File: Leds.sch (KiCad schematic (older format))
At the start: 1 part

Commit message: version preliminar de la etapa de alimentacion
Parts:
- gave numbers to parts that had none: 1
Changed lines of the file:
@@
 LIBS:Sensores
 LIBS:Reles
+LIBS:Reguladores
+LIBS:Transistores
 LIBS:Wifi_PB-cache
 EELAYER 26 0
@@
 $Descr A4 11693 8268
 encoding utf-8
-Sheet 9 11
+Sheet 9 15
 Title ""
 Date "2017-01-15"
@@
 $EndDescr
 $Comp
-L R R?
+L R R38
 U 1 1 587C019B
 P 5250 3800
-F 0 "R?" H 5320 3846 50  0000 L CNN
+F 0 "R38" H 5320 3846 50  0000 L CNN
 F 1 "R" H 5320 3755 50  0000 L CNN
-F 2 "" V 5180 3800 50  0000 C CNN
+F 2 "" V 5180 3800 50  0001 C CNN
 F 3 "" H 5250 3800 50  0000 C CNN
 	1    5250 3800

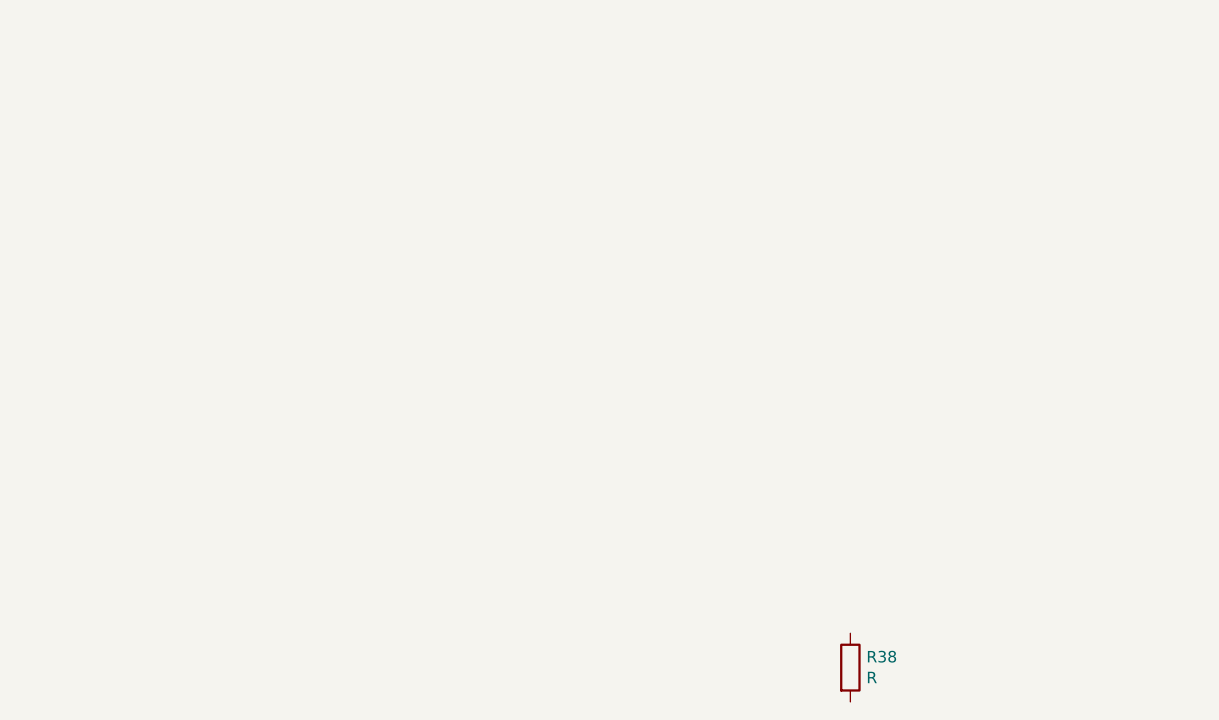
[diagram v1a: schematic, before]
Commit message: asignacion inicial de huellas
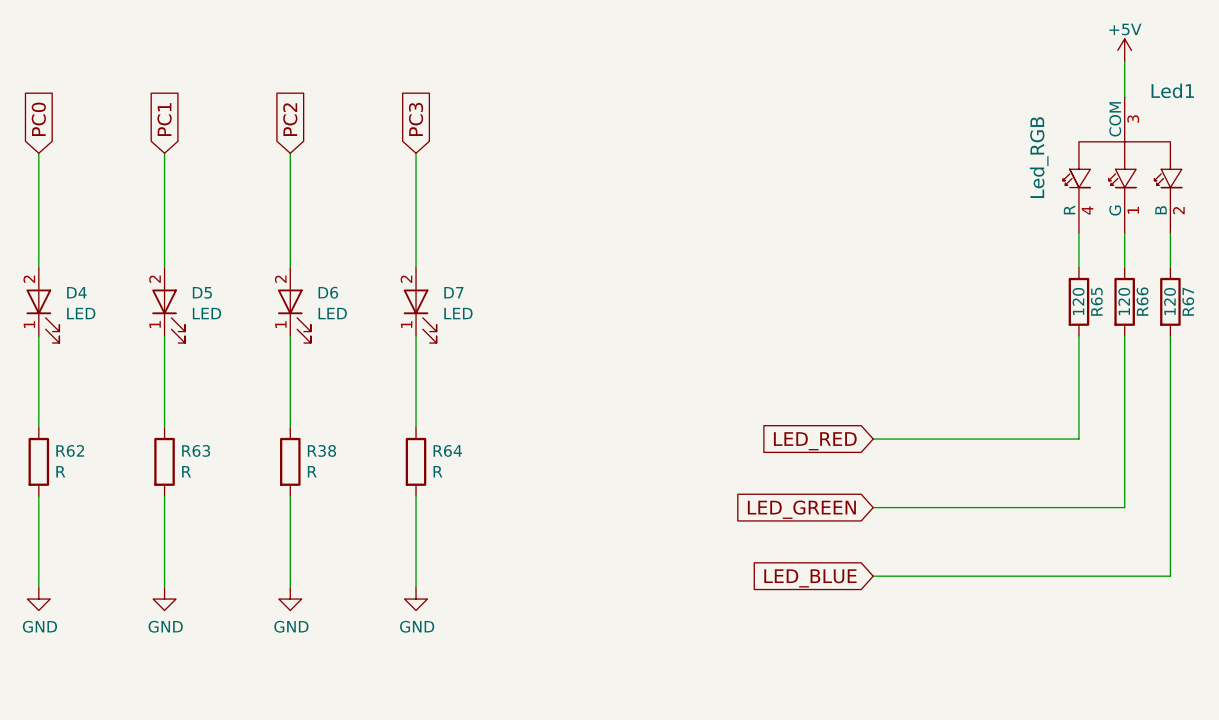
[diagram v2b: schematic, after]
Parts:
- added D4, D5, D6, D7: LED, LEDs:LED_0805, symbol LED
- added Led1: Led_RGB, Leds:LED_RGB_5mm_G_B_COM_R_Anodo_comun, symbol Led_RGB_Anodo_Comun
- added R62, R63, R64: R, Resistencias:R_0805, symbol R
- added R65, R66, R67: 120, Resistencias:R_0805, symbol R
- R38: footprint (none) -> Resistencias:R_0805
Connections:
- net at R38.1: now also D6.1 (K)
- net GND: now reaches R38.2
- net GND: now also R62.2, R63.2, R64.2
- new net: D7.1 (K), R64.1
- new net: D4.1 (K), R62.1
- new net: D5.1 (K), R63.1
- new net: Led1.1 (G), R66.1
- new net: Led1.2 (B), R67.1
- new net: Led1.4 (R), R65.1
- new net +5V: Led1.3 (COM)
- new net LED_BLUE: R67.2
- new net LED_GREEN: R66.2
- new net LED_RED: R65.2
- new net PC0: D4.2 (A)
- new net PC1: D5.2 (A)
- new net PC2: D6.2 (A)
- new net PC3: D7.2 (A)
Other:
- moved on the sheet: R38

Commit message: place inicial sobre la pcb
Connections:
- net GND: now also D4.1 (K), D5.1 (K), D6.1 (K), D7.1 (K); no longer R38.2, R62.2, R63.2, R64.2
- net PC0: now also R62.1; no longer D4.2 (A)
- net PC1: now also R63.1; no longer D5.2 (A)
- net PC2: now also R38.1; no longer D6.2 (A)
- net PC3: now also R64.1; no longer D7.2 (A)
- new net: D6.2 (A), R38.2
- new net: D7.2 (A), R64.2
- new net: D4.2 (A), R62.2
- new net: D5.2 (A), R63.2
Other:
- moved on the sheet: D4, D5, D6, D7, R38, R62, R63, R64
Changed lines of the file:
@@
 L R R38
 U 1 1 587C019B
-P 2800 2900
-F 0 "R38" H 2870 2946 50  0000 L CNN
-F 1 "R" H 2870 2855 50  0000 L CNN
-F 2 "Resistencias:R_0805" V 2730 2900 50  0001 C CNN
-F 3 "" H 2800 2900 50  0000 C CNN
-	1    2800 2900
+P 2800 2200
+F 0 "R38" H 2870 2246 50  0000 L CNN
+F 1 "R" H 2870 2155 50  0000 L CNN
+F 2 "Resistencias:R_0805" V 2730 2200 50  0001 C CNN
+F 3 "" H 2800 2200 50  0000 C CNN
+	1    2800 2200
 	1    0    0    -1
 $EndComp
@@
 L LED D6
 U 1 1 58911235
-P 2800 2200
-F 0 "D6" V 2838 2083 50  0000 R CNN
-F 1 "LED" V 2747 2083 50  0000 R CNN
-F 2 "LEDs:LED_0805" H 2800 2200 50  0001 C CNN
-F 3 "" H 2800 2200 50  0001 C CNN
-	1    2800 2200
+P 2800 2900
+F 0 "D6" V 2838 2783 50  0000 R CNN
+F 1 "LED" V 2747 2783 50  0000 R CNN
+F 2 "LEDs:LED_0805" H 2800 2900 50  0001 C CNN
+F 3 "" H 2800 2900 50  0001 C CNN
+	1    2800 2900
 	0    -1   -1   0
 $EndComp
@@
 L R R64
 U 1 1 5891178E
-P 3350 2900
-F 0 "R64" H 3420 2946 50  0000 L CNN
-F 1 "R" H 3420 2855 50  0000 L CNN
-F 2 "Resistencias:R_0805" V 3280 2900 50  0001 C CNN
-F 3 "" H 3350 2900 50  0000 C CNN
-	1    3350 2900
+P 3350 2200
+F 0 "R64" H 3420 2246 50  0000 L CNN
+F 1 "R" H 3420 2155 50  0000 L CNN
+F 2 "Resistencias:R_0805" V 3280 2200 50  0001 C CNN
+F 3 "" H 3350 2200 50  0000 C CNN
+	1    3350 2200
 	1    0    0    -1
 $EndComp
@@
 L LED D7
 U 1 1 58911795
-P 3350 2200
-F 0 "D7" V 3388 2083 50  0000 R CNN
-F 1 "LED" V 3297 2083 50  0000 R CNN
-F 2 "LEDs:LED_0805" H 3350 2200 50  0001 C CNN
-F 3 "" H 3350 2200 50  0001 C CNN
-	1    3350 2200
+P 3350 2900
+F 0 "D7" V 3388 2783 50  0000 R CNN
+F 1 "LED" V 3297 2783 50  0000 R CNN
+F 2 "LEDs:LED_0805" H 3350 2900 50  0001 C CNN
+F 3 "" H 3350 2900 50  0001 C CNN
+	1    3350 2900
 	0    -1   -1   0
 $EndComp
@@
 L R R62
 U 1 1 589119C4
-P 1700 2900
-F 0 "R62" H 1770 2946 50  0000 L CNN
-F 1 "R" H 1770 2855 50  0000 L CNN
-F 2 "Resistencias:R_0805" V 1630 2900 50  0001 C CNN
-F 3 "" H 1700 2900 50  0000 C CNN
-	1    1700 2900
+P 1700 2200
+F 0 "R62" H 1770 2246 50  0000 L CNN
+F 1 "R" H 1770 2155 50  0000 L CNN
+F 2 "Resistencias:R_0805" V 1630 2200 50  0001 C CNN
+F 3 "" H 1700 2200 50  0000 C CNN
+	1    1700 2200
 	1    0    0    -1
 $EndComp
@@
 L LED D4
 U 1 1 589119CB
-P 1700 2200
-F 0 "D4" V 1738 2083 50  0000 R CNN
-F 1 "LED" V 1647 2083 50  0000 R CNN
-F 2 "LEDs:LED_0805" H 1700 2200 50  0001 C CNN
-F 3 "" H 1700 2200 50  0001 C CNN
-	1    1700 2200
+P 1700 2900
+F 0 "D4" V 1738 2783 50  0000 R CNN
+F 1 "LED" V 1647 2783 50  0000 R CNN
+F 2 "LEDs:LED_0805" H 1700 2900 50  0001 C CNN
+F 3 "" H 1700 2900 50  0001 C CNN
+	1    1700 2900
 	0    -1   -1   0
 $EndComp
@@
 L R R63
 U 1 1 589119D2
-P 2250 2900
-F 0 "R63" H 2320 2946 50  0000 L CNN
-F 1 "R" H 2320 2855 50  0000 L CNN
-F 2 "Resistencias:R_0805" V 2180 2900 50  0001 C CNN
-F 3 "" H 2250 2900 50  0000 C CNN
-	1    2250 2900
+P 2250 2200
+F 0 "R63" H 2320 2246 50  0000 L CNN
+F 1 "R" H 2320 2155 50  0000 L CNN
+F 2 "Resistencias:R_0805" V 2180 2200 50  0001 C CNN
+F 3 "" H 2250 2200 50  0000 C CNN
+	1    2250 2200
 	1    0    0    -1
 $EndComp
@@
 L LED D5
 U 1 1 589119D9
-P 2250 2200
-F 0 "D5" V 2288 2083 50  0000 R CNN
-F 1 "LED" V 2197 2083 50  0000 R CNN
-F 2 "LEDs:LED_0805" H 2250 2200 50  0001 C CNN
-F 3 "" H 2250 2200 50  0001 C CNN
-	1    2250 2200
+P 2250 2900
+F 0 "D5" V 2288 2783 50  0000 R CNN
+F 1 "LED" V 2197 2783 50  0000 R CNN
+F 2 "LEDs:LED_0805" H 2250 2900 50  0001 C CNN
+F 3 "" H 2250 2900 50  0001 C CNN
+	1    2250 2900
 	0    -1   -1   0
 $EndComp
@@
 	3350 2750 3350 2350
 $Comp
-L GND #PWR092
+L GND #PWR089
 U 1 1 58911F78
 P 1700 3450
-F 0 "#PWR092" H 1700 3200 50  0001 C CNN
+F 0 "#PWR089" H 1700 3200 50  0001 C CNN
 F 1 "GND" H 1705 3277 50  0000 C CNN
 F 2 "" H 1700 3450 50  0001 C CNN
@@
 $EndComp
 $Comp
-L GND #PWR093
+L GND #PWR090
 U 1 1 58911FA2
 P 2250 3450
-F 0 "#PWR093" H 2250 3200 50  0001 C CNN
+F 0 "#PWR090" H 2250 3200 50  0001 C CNN
 F 1 "GND" H 2255 3277 50  0000 C CNN
 F 2 "" H 2250 3450 50  0001 C CNN
@@
 $EndComp
 $Comp
-L GND #PWR094
+L GND #PWR091
 U 1 1 58911FC5
 P 2800 3450
-F 0 "#PWR094" H 2800 3200 50  0001 C CNN
+F 0 "#PWR091" H 2800 3200 50  0001 C CNN
 F 1 "GND" H 2805 3277 50  0000 C CNN
 F 2 "" H 2800 3450 50  0001 C CNN
@@
 $EndComp
 $Comp
-L GND #PWR095
+L GND #PWR092
 U 1 1 58911FE8
 P 3350 3450
-F 0 "#PWR095" H 3350 3200 50  0001 C CNN
+F 0 "#PWR092" H 3350 3200 50  0001 C CNN
 F 1 "GND" H 3355 3277 50  0000 C CNN
 F 2 "" H 3350 3450 50  0001 C CNN
@@
 $EndComp
 $Comp
-L +5V #PWR096
+L +5V #PWR093
 U 1 1 58919BA3
 P 6450 1150
-F 0 "#PWR096" H 6450 1000 50  0001 C CNN
+F 0 "#PWR093" H 6450 1000 50  0001 C CNN
 F 1 "+5V" H 6450 1290 50  0000 C CNN
 F 2 "" H 6450 1150 50  0000 C CNN
